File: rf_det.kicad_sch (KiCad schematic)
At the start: 16 parts, among them U2 AD8318ACPZ-REEL7, U3 AD8318ACPZ-REEL7

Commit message: Add files via upload
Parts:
- renumbered C9 to C39, C10 to C40, C11 to C41, C12 to C42, C13 to C43, C14 to C44, C15 to C45, C16 to C46, C17 to C47, FB2 to FB3, R18 to R26, R19 to R27, R20 to R28, R21 to R29
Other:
- moved on the sheet: C39, C42, C44

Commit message: Add files via upload
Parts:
- renumbered C39 to C58, C40 to C59, C41 to C60, C42 to C61, C43 to C62, C44 to C63, C45 to C64, C46 to C65, C47 to C66, FB3 to FB4, R26 to R30, R27 to R31, R28 to R32, R29 to R33

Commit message: Add files via upload
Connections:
- net RF_FWD_DET renamed FWD_SENSE_OUT
- net RF_FWD_IN renamed FWD_RF_IN
- net RF_REF_DET renamed REF_SENSE_OUT
- net RF_REF_IN renamed REF_RF_IN
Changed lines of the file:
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@@
     (effects (font (size 1.27 1.27)) (justify right))
   )
-  (hierarchical_label "RF_REF_DET" (shape output) (at 297.18 135.89 0) (fields_autoplaced)
+  (hierarchical_label "REF_SENSE_OUT" (shape output) (at 297.18 135.89 0) (fields_autoplaced)
     (effects (font (size 1.27 1.27)) (justify left))
   )
-  (hierarchical_label "RF_FWD_DET" (shape output) (at 132.08 135.89 0) (fields_autoplaced)
+  (hierarchical_label "FWD_SENSE_OUT" (shape output) (at 132.08 135.89 0) (fields_autoplaced)
     (effects (font (size 1.27 1.27)) (justify left))
   )
-  (hierarchical_label "RF_REF_IN" (shape input) (at 298.45 60.96 90) (fields_autoplaced)
+  (hierarchical_label "REF_RF_IN" (shape input) (at 298.45 60.96 90) (fields_autoplaced)
     (effects (font (size 1.27 1.27)) (justify left))
   )
-  (hierarchical_label "RF_FWD_IN" (shape input) (at 133.35 60.96 90) (fields_autoplaced)
+  (hierarchical_label "FWD_RF_IN" (shape input) (at 133.35 60.96 90) (fields_autoplaced)
     (effects (font (size 1.27 1.27)) (justify left))
   )

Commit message: Add files via upload
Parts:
- renumbered R30 to R33, R31 to R34, R32 to R35, R33 to R36
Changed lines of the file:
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@@
   (symbol (lib_id "Device:R_Small") (at 152.4 106.68 90) (unit 1)
     (in_bom yes) (on_board yes) (dnp no)
-    (property "Reference" "R31" (at 152.4 104.14 90)
+    (property "Reference" "R34" (at 152.4 104.14 90)
       (effects (font (size 1.27 1.27)))
     )
@@
       (project "m17-rru-rf"
         (path "/4c42207c-9e6b-42da-ad38-da126b892014/ccc39fee-262d-4ac9-a9a6-59e024db6eed"
-          (reference "R31") (unit 1)
+          (reference "R34") (unit 1)
         )
       )
@@
   (symbol (lib_id "Device:R_Small") (at 294.64 67.31 90) (unit 1)
     (in_bom yes) (on_board yes) (dnp no) (fields_autoplaced)
-    (property "Reference" "R32" (at 294.64 62.4291 90)
+    (property "Reference" "R35" (at 294.64 62.4291 90)
       (effects (font (size 1.27 1.27)))
     )
@@
       (project "m17-rru-rf"
         (path "/4c42207c-9e6b-42da-ad38-da126b892014/ccc39fee-262d-4ac9-a9a6-59e024db6eed"
-          (reference "R32") (unit 1)
+          (reference "R35") (unit 1)
         )
       )
@@
   (symbol (lib_id "Device:R_Small") (at 129.54 67.31 90) (unit 1)
     (in_bom yes) (on_board yes) (dnp no) (fields_autoplaced)
-    (property "Reference" "R30" (at 129.54 62.4291 90)
+    (property "Reference" "R33" (at 129.54 62.4291 90)
       (effects (font (size 1.27 1.27)))
     )
@@
       (project "m17-rru-rf"
         (path "/4c42207c-9e6b-42da-ad38-da126b892014/ccc39fee-262d-4ac9-a9a6-59e024db6eed"
-          (reference "R30") (unit 1)
+          (reference "R33") (unit 1)
         )
       )
@@
   (symbol (lib_id "Device:R_Small") (at 317.5 106.68 90) (unit 1)
     (in_bom yes) (on_board yes) (dnp no)
-    (property "Reference" "R33" (at 317.5 104.14 90)
+    (property "Reference" "R36" (at 317.5 104.14 90)
       (effects (font (size 1.27 1.27)))
     )
@@
       (project "m17-rru-rf"
         (path "/4c42207c-9e6b-42da-ad38-da126b892014/ccc39fee-262d-4ac9-a9a6-59e024db6eed"
-          (reference "R33") (unit 1)
-        )
-      )
+          (reference "R36") (unit 1)
+        )
+      )

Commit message: partial PN update
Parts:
- C59: renamed from C58; PN (none) -> CL10B105KB8NQNC
- C60: renamed from C59; PN (none) -> C0603C104M5RAC7411
- C61: renamed from C60; PN (none) -> C0603C102J5GAC7411
- C62: renamed from C61; PN (none) -> C0603C104M5RAC7411
- C63: renamed from C62; PN (none) -> C0603C102J5GAC7411
- C64: renamed from C63; PN (none) -> C0603C102J5GAC7411
- C65: renamed from C64; PN (none) -> C0603C104M5RAC7411
- C66: renamed from C65; PN (none) -> C0603C102J5GAC7411
- C67: renamed from C66; PN (none) -> C0603C102J5GAC7411

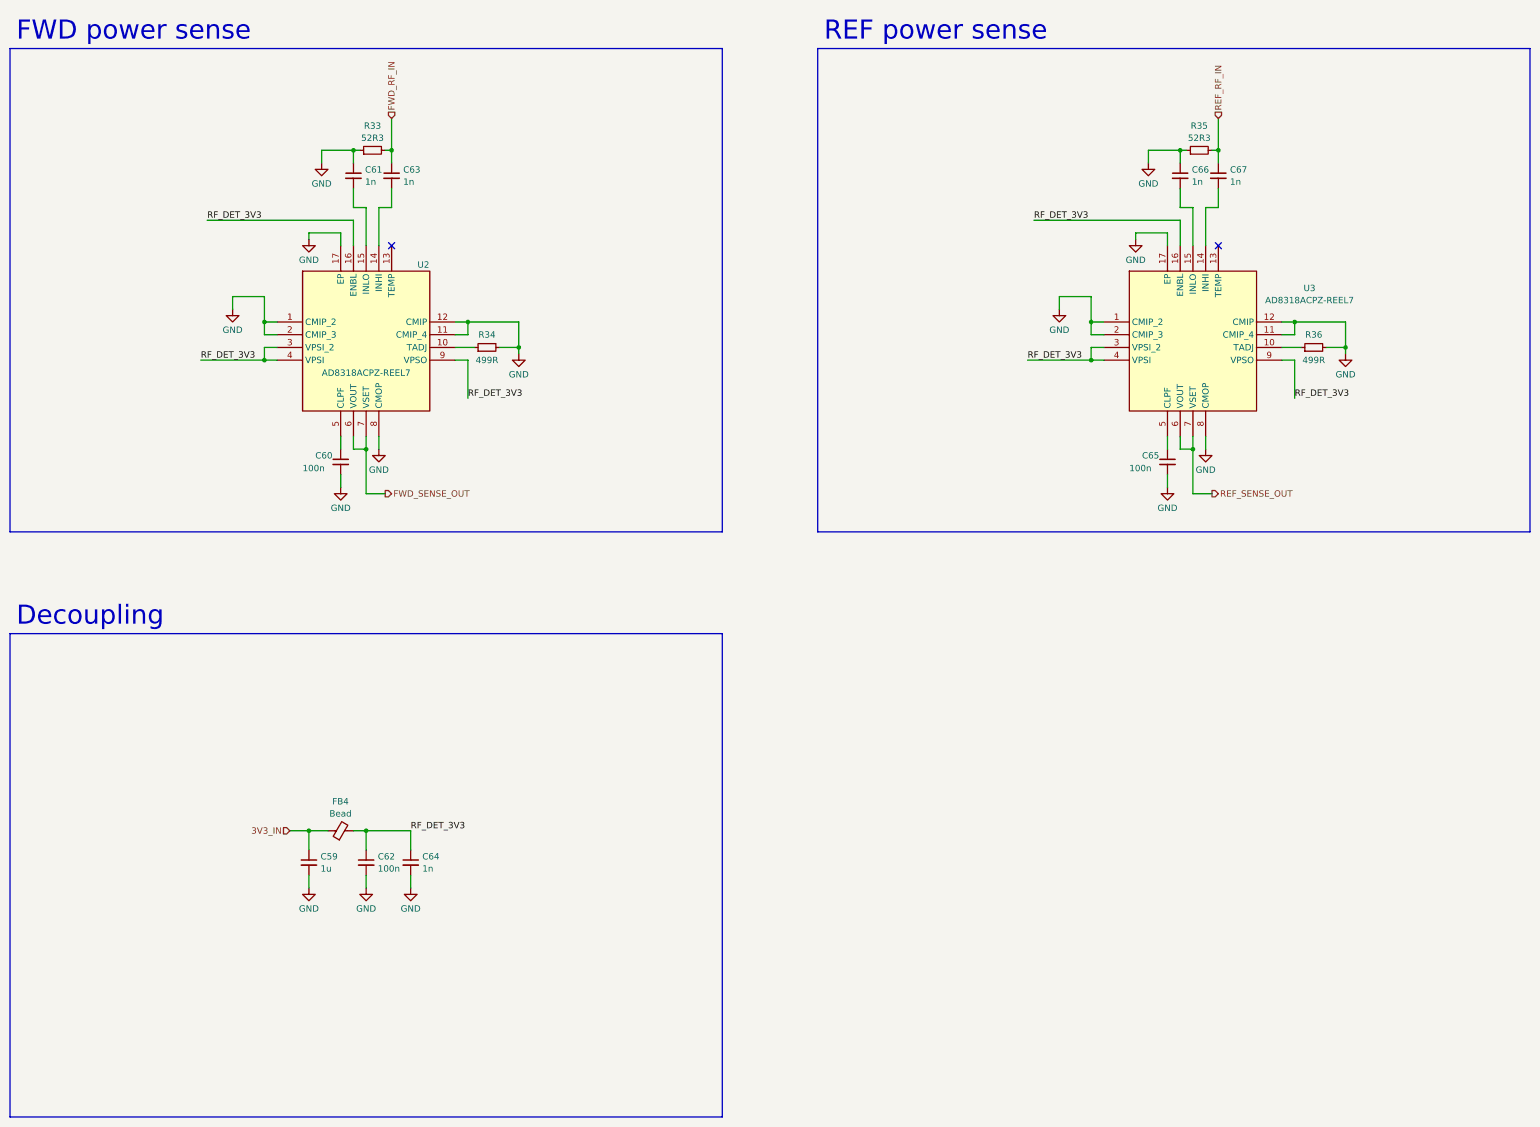
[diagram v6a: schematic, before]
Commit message: added missing 40MHz source
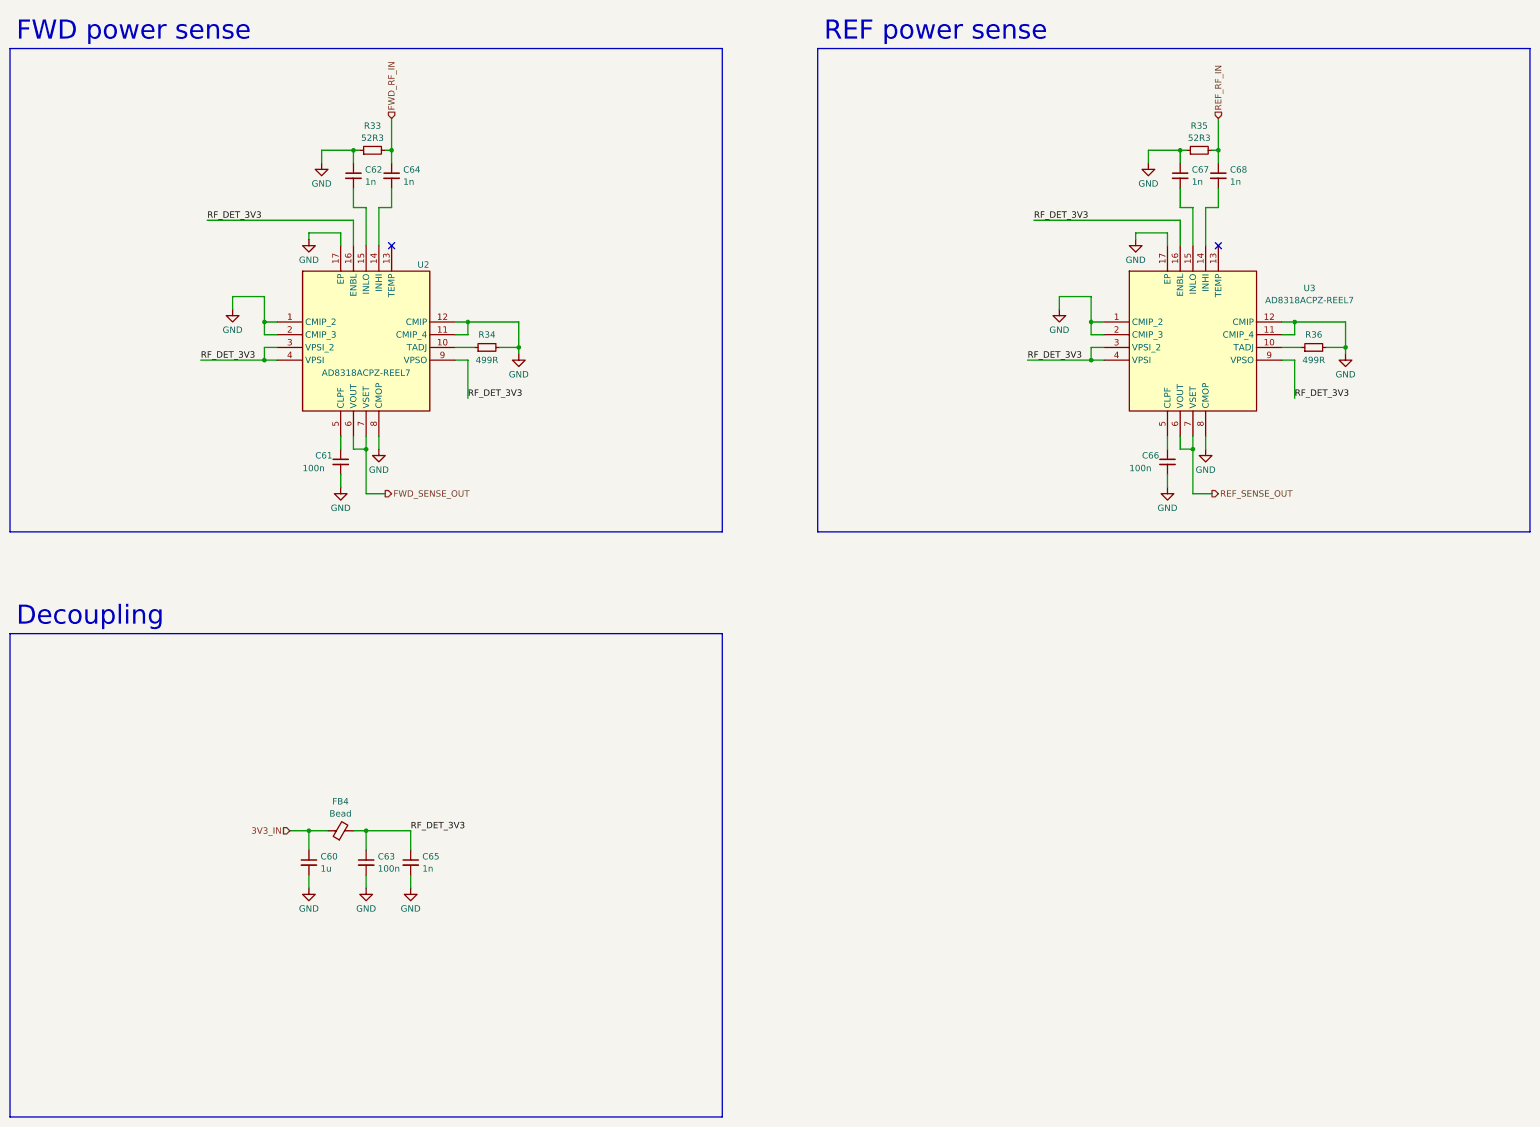
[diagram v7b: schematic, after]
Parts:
- renumbered C59 to C60, C60 to C61, C61 to C62, C62 to C63, C63 to C64, C64 to C65, C65 to C66, C66 to C67, C67 to C68

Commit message: significant updates
- supply for the detector block changed from 3.3V to 5V
- minor bugfixes
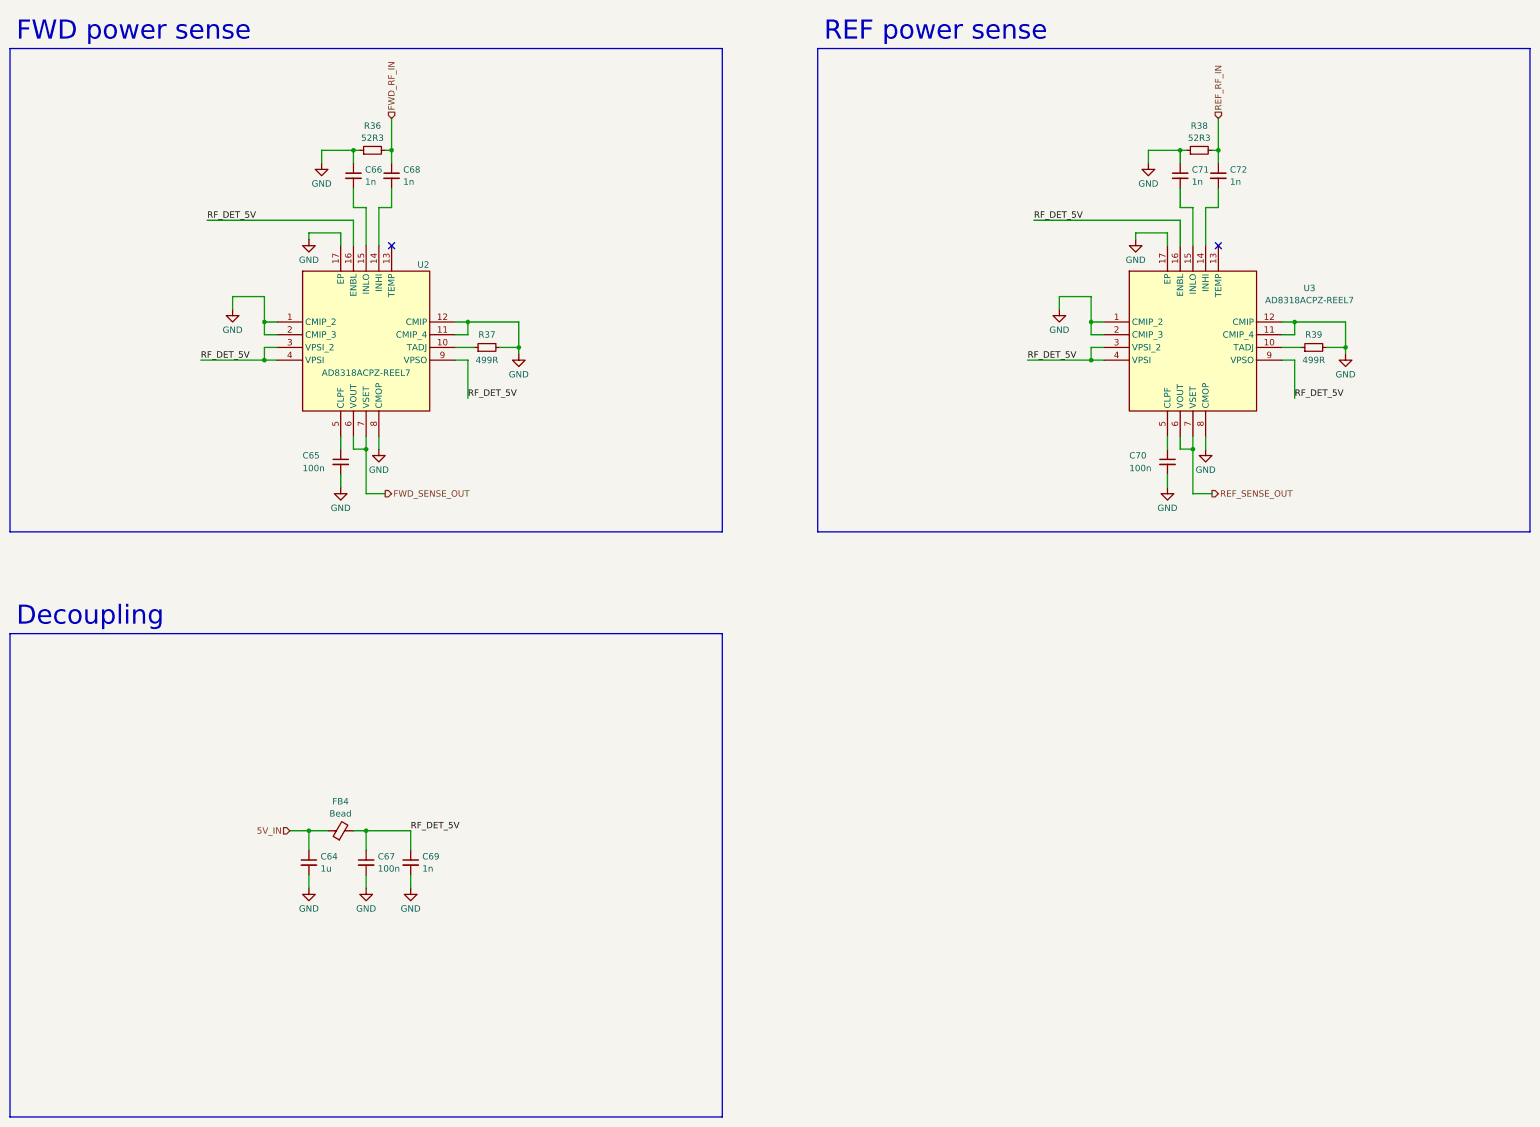
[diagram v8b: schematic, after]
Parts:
- renumbered C60 to C64, C61 to C65, C62 to C66, C63 to C67, C64 to C68, C65 to C69, C66 to C70, C67 to C71, C68 to C72, R33 to R36, R34 to R37, R35 to R38, R36 to R39
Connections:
- net 3V3_IN renamed 5V_IN
- net RF_DET_3V3 renamed RF_DET_5V
